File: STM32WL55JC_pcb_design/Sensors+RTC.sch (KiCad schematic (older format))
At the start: 19 parts, among them IC6 HTS221TR, U1 DS1307+, U2 L80-M39, U3 LIS3DHTR, Y4 32.768kHz

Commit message: Finish pcb routing
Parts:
- removed C49, C53: 100nF, Capacitor_SMD:C_0805_2012Metric, symbol pspice:CAP
- removed C50, C52: 15pF, Capacitor_SMD:C_0805_2012Metric, symbol Device:C_Small
- removed C51, C54: 10uF, Capacitor_SMD:C_0805_2012Metric, symbol pspice:CAP
- removed U1: DS1307+, Package_DIP:DIP-8_W7.62mm, symbol Timer_RTC:DS1307+
- removed Y4: 32.768kHz, SC20S-12.5PF20PPM:SC20S125PF20PPM, symbol Device:Crystal
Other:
- moved on the sheet: C55, C56, C57, C58, C59, C60, IC6, R10, R11, U2, U3

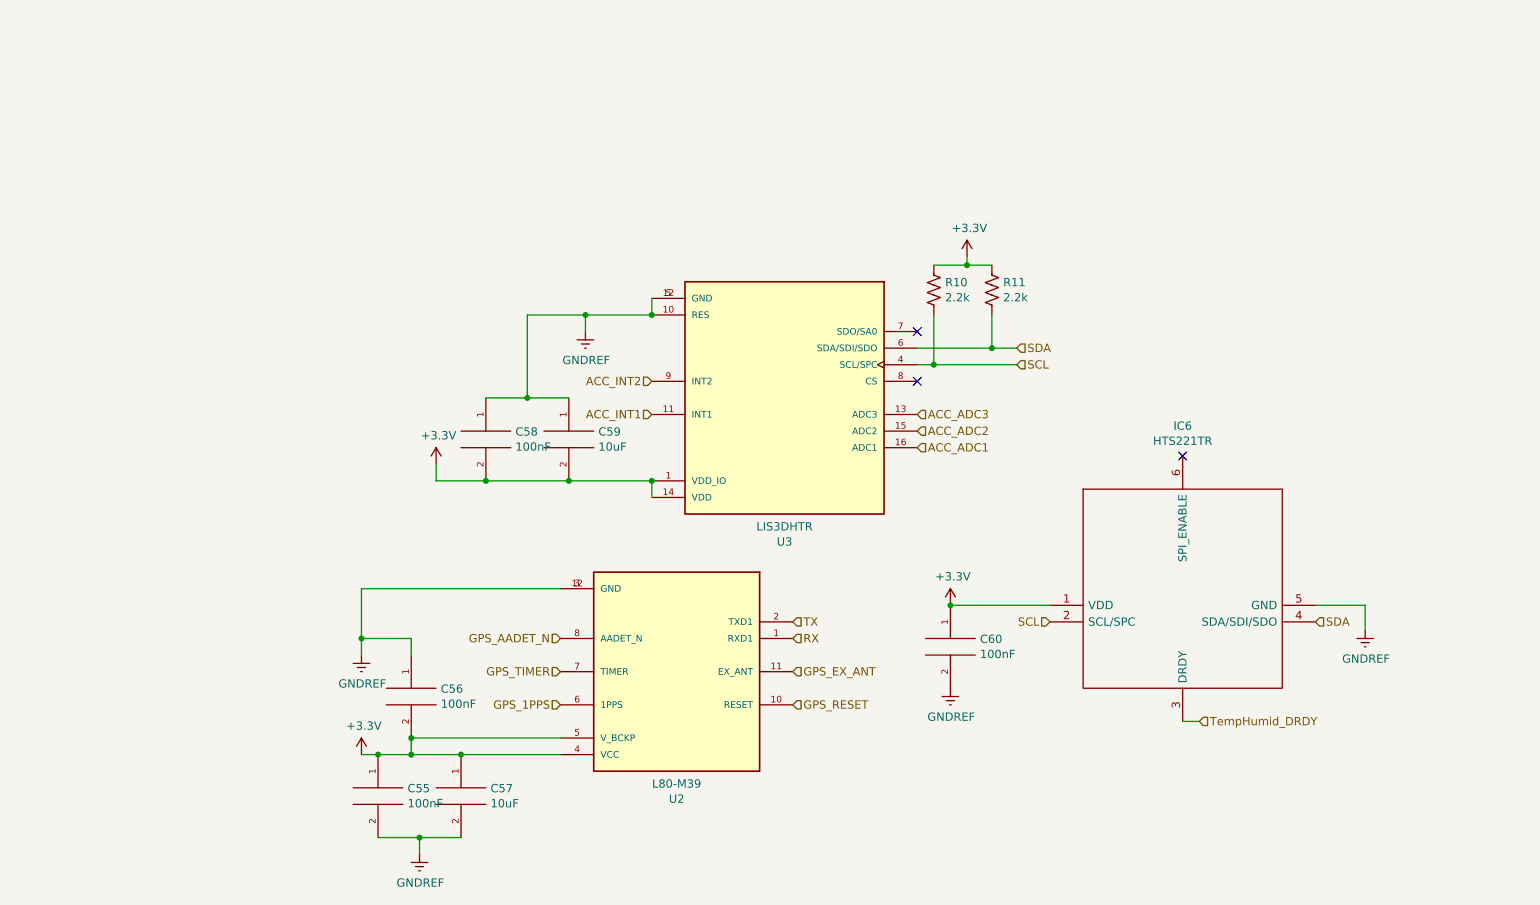
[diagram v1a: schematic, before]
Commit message: Change devices to available ones from JLC
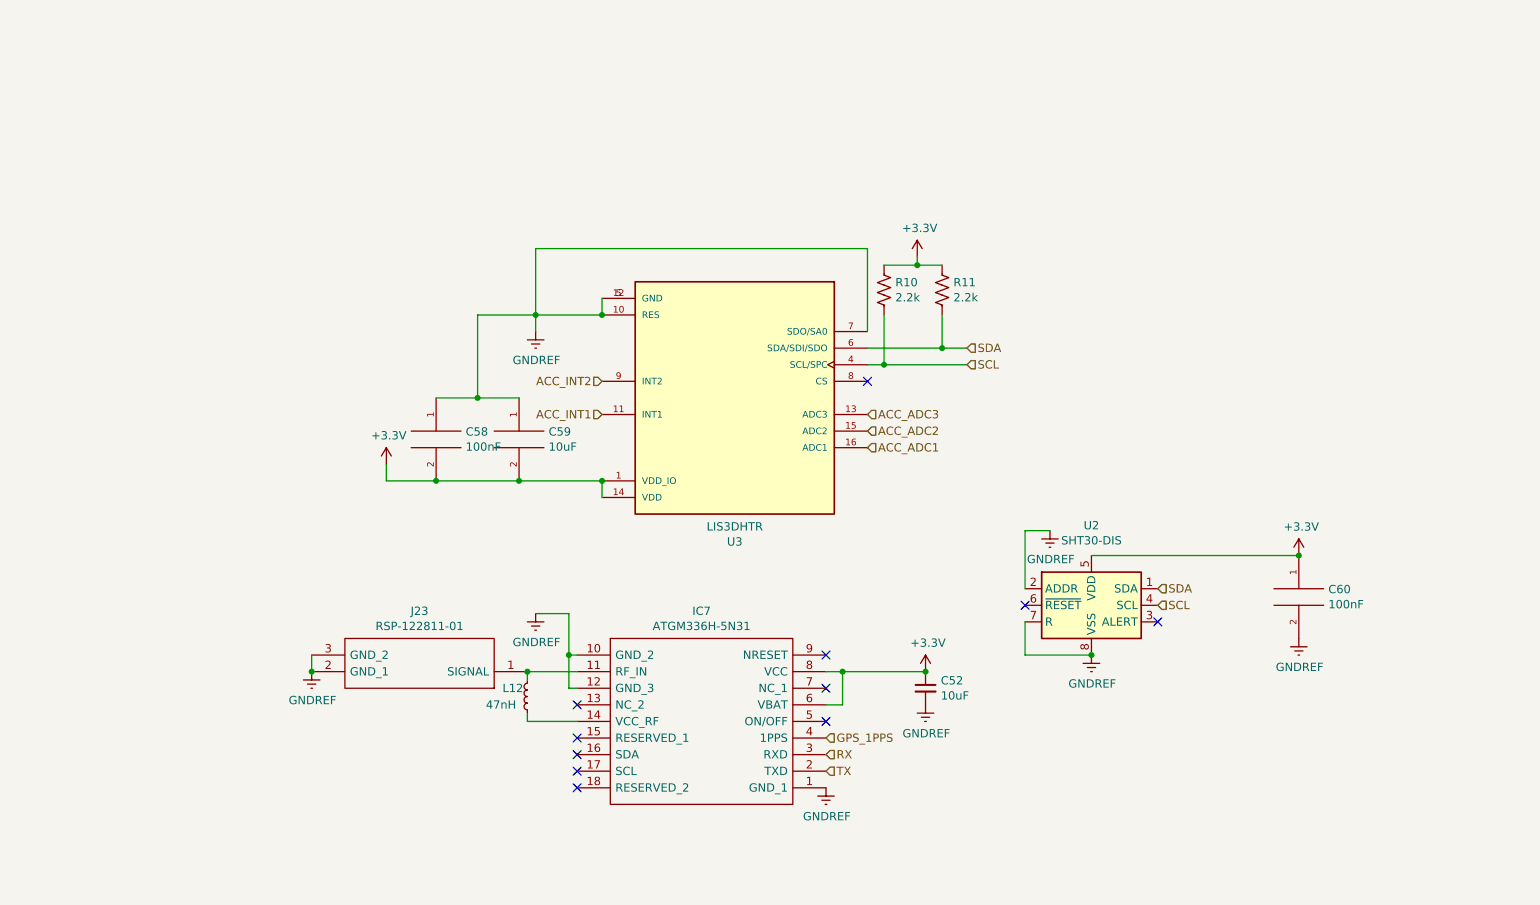
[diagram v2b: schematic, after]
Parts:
- removed C55, C56: 100nF, Capacitor_SMD:C_0805_2012Metric, symbol pspice:CAP
- removed C57: 10uF, Capacitor_SMD:C_0805_2012Metric, symbol pspice:CAP
- removed IC6: HTS221TR, HTS221TR:HTS221TR, symbol HTS221TR:HTS221TR
- removed U2: L80-M39, L80-M39:XCVR_L80-M39, symbol STM32WL55JC_pcb_design-rescue:L80-M39-L80-M39
- added C52: 10uF, Capacitor_SMD:C_0805_2012Metric, symbol Device:C_Small
- added IC7: ATGM336H-5N31, ATGM336H-5N31:ATGM336H5N31, symbol ATGM336H-5N31:ATGM336H-5N31
- added J23: RSP-122811-01, HC-RF-IPEX0303:RSP12281101, symbol HC-RF-IPEX0303:RSP-122811-01
- added L12: 47nH, Inductor_SMD:L_0805_2012Metric, symbol Device:L_Small
- added U2: SHT30-DIS, Sensor_Humidity:Sensirion_DFN-8-1EP_2.5x2.5mm_P0.5mm_EP1.1x1.7mm, symbol Sensor_Humidity:SHT30-DIS
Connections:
- net +3V3: now also C52.1, IC7.6 (VBAT), IC7.8 (VCC), U2.5 (VDD)
- net GNDREF: now also U3.7 (SDO/SA0), C52.2, IC7.1 (GND_1), IC7.10 (GND_2), IC7.12 (GND_3), J23.2 (GND_1), J23.3 (GND_2), U2.2 (ADDR), U2.7 (R), U2.8 (VSS), U2.9 (VSS)
- net GPS_1PPS: now also IC7.4 (1PPS)
- net RX: now also IC7.3 (RXD)
- net SCL: now also U2.4 (SCL)
- net SDA: now also U2.1 (SDA)
- net TX: now also IC7.2 (TXD)
- new net: IC7.11 (RF_IN), J23.1 (SIGNAL), L12.2
- new net: IC7.14 (VCC_RF), L12.1
- no-connect marks 3 -> 11
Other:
- moved on the sheet: C58, C59, C60, R10, R11, U3

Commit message: Finish silk screen
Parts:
- added TP11: ACC_VDD, TestPoint:TestPoint_Pad_D2.0mm, symbol Connector:TestPoint
- added TP12: GND, TestPoint:TestPoint_Pad_D2.0mm, symbol Connector:TestPoint
- added TP13: Temp_VDD, TestPoint:TestPoint_Pad_D2.0mm, symbol Connector:TestPoint
- added TP14: GPS_GND, TestPoint:TestPoint_Pad_D4.0mm, symbol Connector:TestPoint
- added TP15: GPS_VDD, TestPoint:TestPoint_Pad_D4.0mm, symbol Connector:TestPoint
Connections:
- net GNDREF: now also TP12.1, TP14.1
- new net VDD: TP11.1, TP13.1, TP15.1
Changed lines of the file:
@@
 L power:GNDREF #PWR?
 U 1 1 619ADEBE
-P 5850 5450
+P 5850 5500
 AR Path="/619ADEBE" Ref="#PWR?"  Part="1"
 AR Path="/61317136/619ADEBE" Ref="#PWR065"  Part="1"
-F 0 "#PWR065" H 5850 5200 50  0001 C CNN
-F 1 "GNDREF" H 5855 5277 50  0000 C CNN
-F 2 "" H 5850 5450 50  0001 C CNN
-F 3 "" H 5850 5450 50  0001 C CNN
-	1    5850 5450
+F 0 "#PWR065" H 5850 5250 50  0001 C CNN
+F 1 "GNDREF" H 5855 5327 50  0000 C CNN
+F 2 "" H 5850 5500 50  0001 C CNN
+F 3 "" H 5850 5500 50  0001 C CNN
+	1    5850 5500
 	1    0    0    -1
 $EndComp
@@
 NoConn ~ 7050 4350
 NoConn ~ 7850 4450
+$Comp
+L Connector:TestPoint TP11
+U 1 1 6182B42E
+P 4200 950
+F 0 "TP11" H 4258 1068 50  0000 L CNN
+F 1 "ACC_VDD" H 4258 977 50  0000 L CNN
+F 2 "TestPoint:TestPoint_Pad_D2.0mm" H 4400 950 50  0001 C CNN
+F 3 "~" H 4400 950 50  0001 C CNN
+	1    4200 950
+	1    0    0    -1
+$EndComp
+$Comp
+L Connector:TestPoint TP12
+U 1 1 6182DF32
+P 4650 950
+F 0 "TP12" H 4708 1068 50  0000 L CNN
+F 1 "GND" H 4708 977 50  0000 L CNN
+F 2 "TestPoint:TestPoint_Pad_D2.0mm" H 4850 950 50  0001 C CNN
+F 3 "~" H 4850 950 50  0001 C CNN
+	1    4650 950
+	1    0    0    -1
+$EndComp
+Wire Wire Line
+	5850 5450 5850 5500
+$Comp
+L Connector:TestPoint TP14
+U 1 1 618316B7
+P 5550 950
+F 0 "TP14" H 5608 1068 50  0000 L CNN
+F 1 "GPS_GND" H 5608 977 50  0000 L CNN
+F 2 "TestPoint:TestPoint_Pad_D4.0mm" H 5750 950 50  0001 C CNN
+F 3 "~" H 5750 950 50  0001 C CNN
+	1    5550 950
+	1    0    0    -1
+$EndComp
+$Comp
+L Connector:TestPoint TP15
+U 1 1 61831ADD
+P 6000 950
+F 0 "TP15" H 6058 1068 50  0000 L CNN
+F 1 "GPS_VDD" H 6058 977 50  0000 L CNN
+F 2 "TestPoint:TestPoint_Pad_D4.0mm" H 6200 950 50  0001 C CNN
+F 3 "~" H 6200 950 50  0001 C CNN
+	1    6000 950
+	1    0    0    -1
+$EndComp
+$Comp
+L power:GNDREF #PWR?
+U 1 1 6186EB6A
+P 4650 950
+AR Path="/6186EB6A" Ref="#PWR?"  Part="1"
+AR Path="/61317136/6186EB6A" Ref="#PWR0103"  Part="1"
+F 0 "#PWR0103" H 4650 700 50  0001 C CNN
+F 1 "GNDREF" H 4655 777 50  0000 C CNN
+F 2 "" H 4650 950 50  0001 C CNN
+F 3 "" H 4650 950 50  0001 C CNN
+	1    4650 950
+	1    0    0    -1
+$EndComp
+Text GLabel 4200 950  3    50   Input ~ 0
+VDD
+Text GLabel 5100 950  3    50   Input ~ 0
+VDD
+$Comp
+L power:GNDREF #PWR?
+U 1 1 618717D5
+P 5550 950
+AR Path="/618717D5" Ref="#PWR?"  Part="1"
+AR Path="/61317136/618717D5" Ref="#PWR0104"  Part="1"
+F 0 "#PWR0104" H 5550 700 50  0001 C CNN
+F 1 "GNDREF" H 5555 777 50  0000 C CNN
+F 2 "" H 5550 950 50  0001 C CNN
+F 3 "" H 5550 950 50  0001 C CNN
+	1    5550 950
+	1    0    0    -1
+$EndComp
+Text GLabel 6000 950  3    50   Input ~ 0
+VDD
+$Comp
+L Connector:TestPoint TP13
+U 1 1 6182E7DC
+P 5100 950
+F 0 "TP13" H 5158 1068 50  0000 L CNN
+F 1 "Temp_VDD" H 5158 977 50  0000 L CNN
+F 2 "TestPoint:TestPoint_Pad_D2.0mm" H 5300 950 50  0001 C CNN
+F 3 "~" H 5300 950 50  0001 C CNN
+	1    5100 950
+	1    0    0    -1
+$EndComp
 $EndSCHEMATC
